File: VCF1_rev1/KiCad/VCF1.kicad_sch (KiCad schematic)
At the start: 24 parts, among them U2 74HC4053, U3 CEM3350, U4 Opamp_Quad

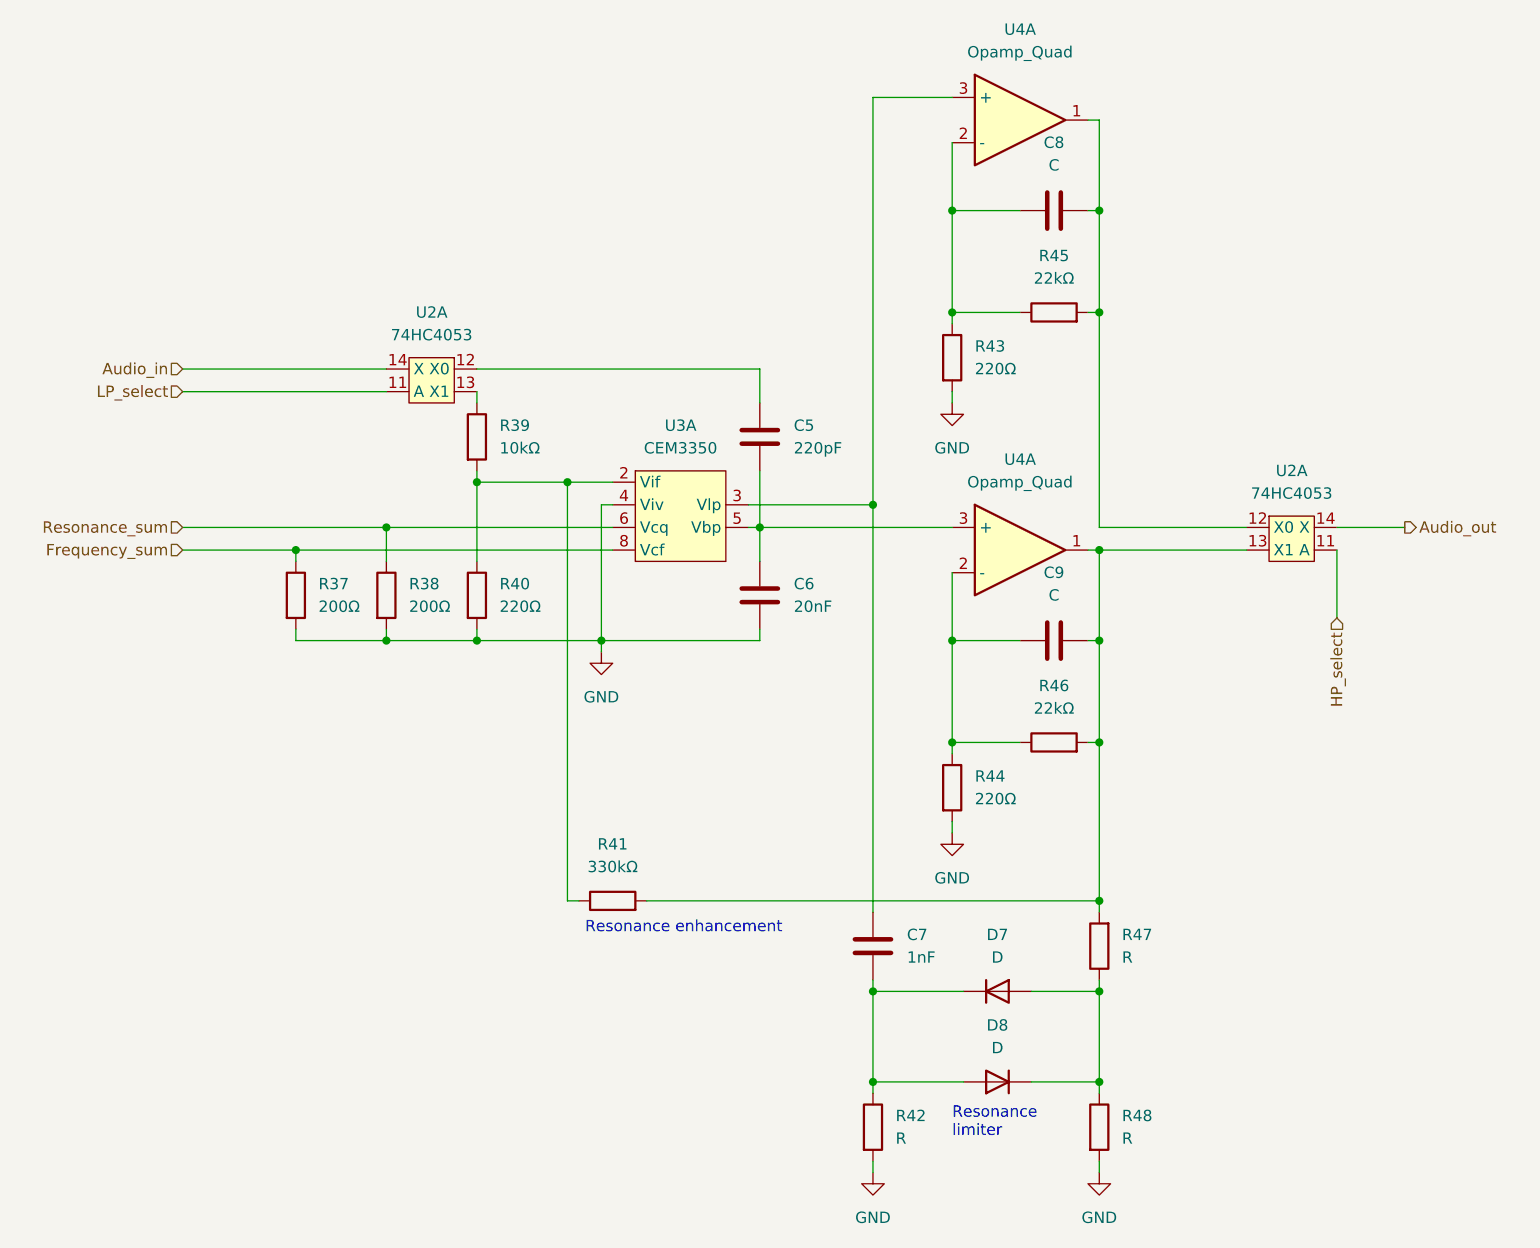
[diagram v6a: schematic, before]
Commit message: Placed more components on the PCB.
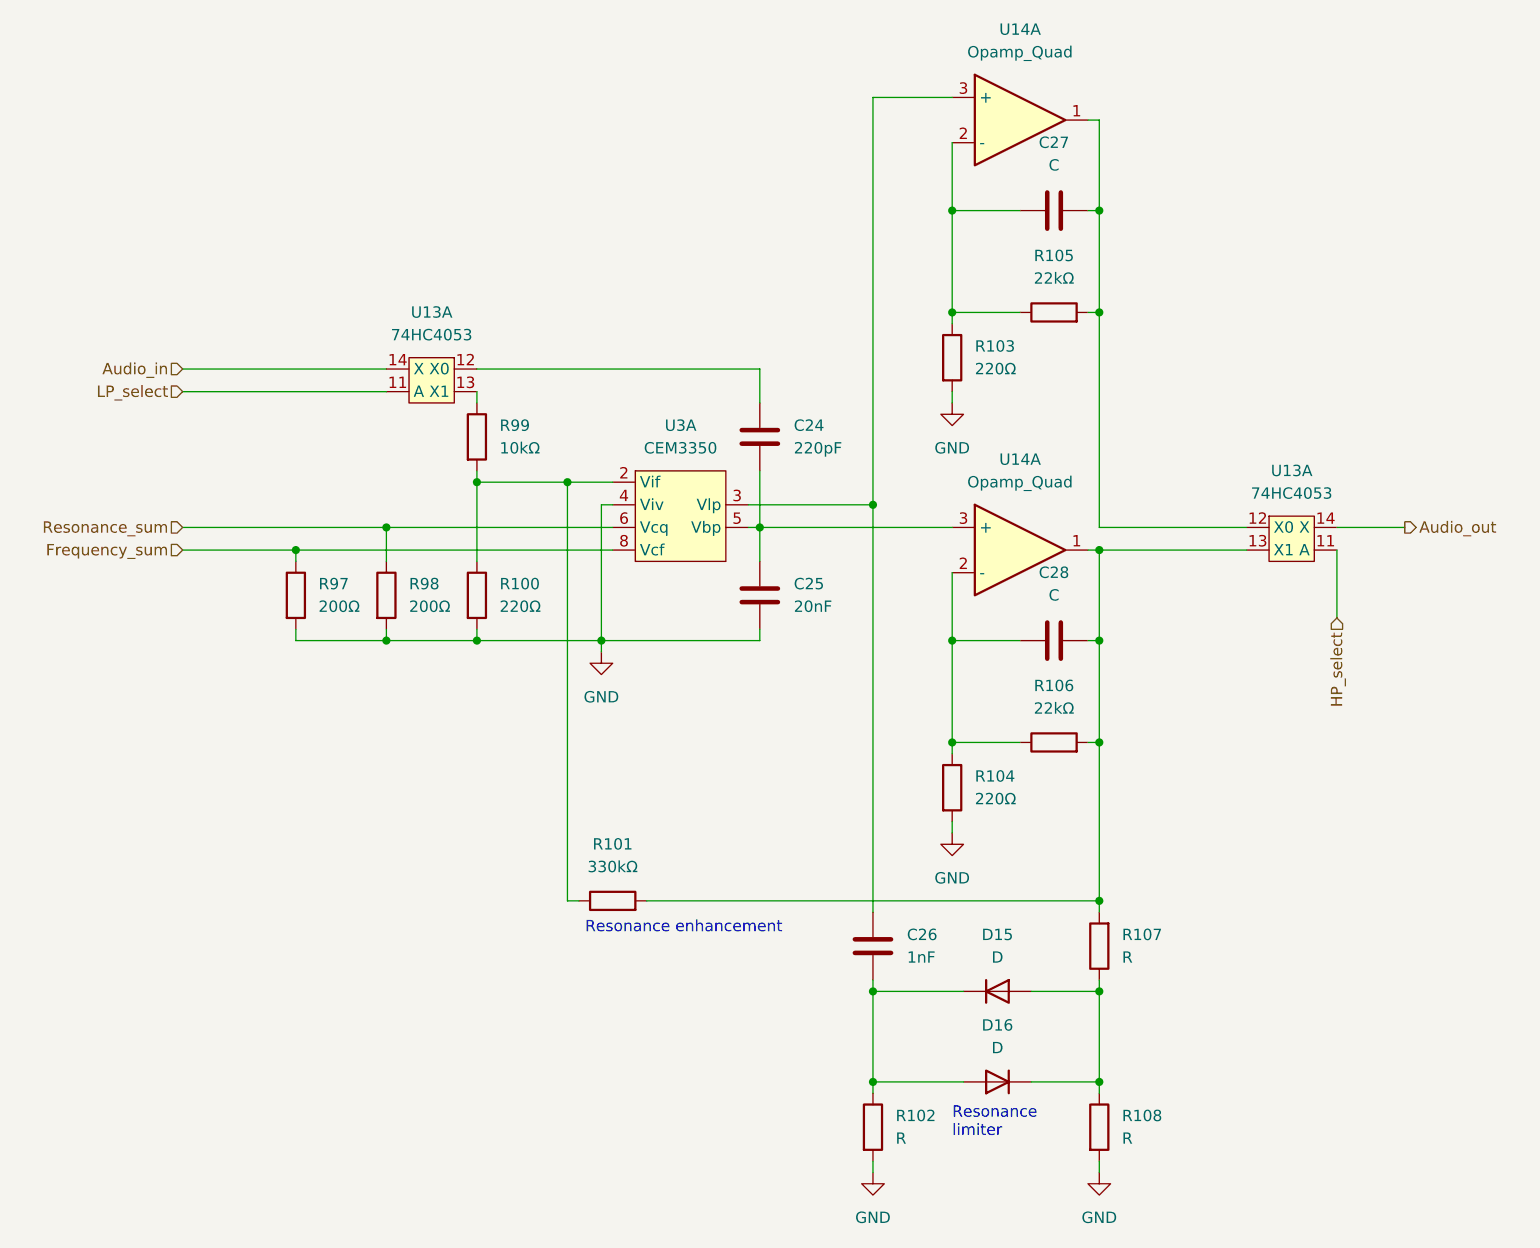
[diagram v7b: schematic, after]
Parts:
- C27: renamed from C8; footprint (none) -> Capacitor_SMD:C_0603_1608Metric
- C28: renamed from C9; footprint (none) -> Capacitor_SMD:C_0603_1608Metric
- renumbered C5 to C24, C6 to C25, C7 to C26, D7 to D15, D8 to D16, R40 to R100, R41 to R101, R42 to R102, R43 to R103, R44 to R104, R45 to R105, R46 to R106, R47 to R107, R48 to R108, R37 to R97, R38 to R98, R39 to R99, U2 to U13, U4 to U14
